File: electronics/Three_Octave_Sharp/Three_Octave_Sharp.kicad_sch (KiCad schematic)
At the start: 156 parts, among them J1 FFC Connector, J1 HRO_TYPE-C-31-M-12, SW1 Key Esc, SW10 Key 9, SW11 Key 0, SW12 Key -, SW13 Key =, SW14 Key \, SW15 Key `, SW16 Key Tab, SW17 Key Q, SW18 Key W, SW19 Key E, SW2 Key 1, SW20 Key R, SW21 Alps_Alpine_SKRP, SW21 Key T, SW22 Alps_Alpine_SKRP, SW22 Key Y, SW23 Key U, SW24 Key I, SW25 Key O, SW26 Key P, SW27 Key [, SW28 Key ], SW29 Key BS, SW3 Key 2, SW30 Key Caps, SW31 Key A, SW32 Key S, SW33 Key D, SW34 Key F, SW35 Key G, SW36 Key H, SW37 Key J, SW38 Key K, SW39 Key L, SW4 Key 3, SW40 Key ;, SW41 Key ', SW42 Key Return, SW43 Key Shift, SW44 Key Z, SW45 Key X, SW46 Key C, SW47 Key V, SW48 Key B, SW49 Key N, SW5 Key 4, SW50 Key M, SW51 Key ,, SW52 Key ., SW53 Key /, SW54 Key Shift, SW55 Key Fn, SW56 Key Ctrl, SW57 Key Opt, SW58 Key Cmd, SW59 Key Space, SW6 Key 5, SW60 Key Cmd, SW61 Key MO(1), SW7 Key 6, SW8 Key 7, SW9 Key 8, U1 AP2112K-3.3, U2 Raspberry_Pi_RP2040, U2 W25Q64JVXGIQ, Y1 12MHz

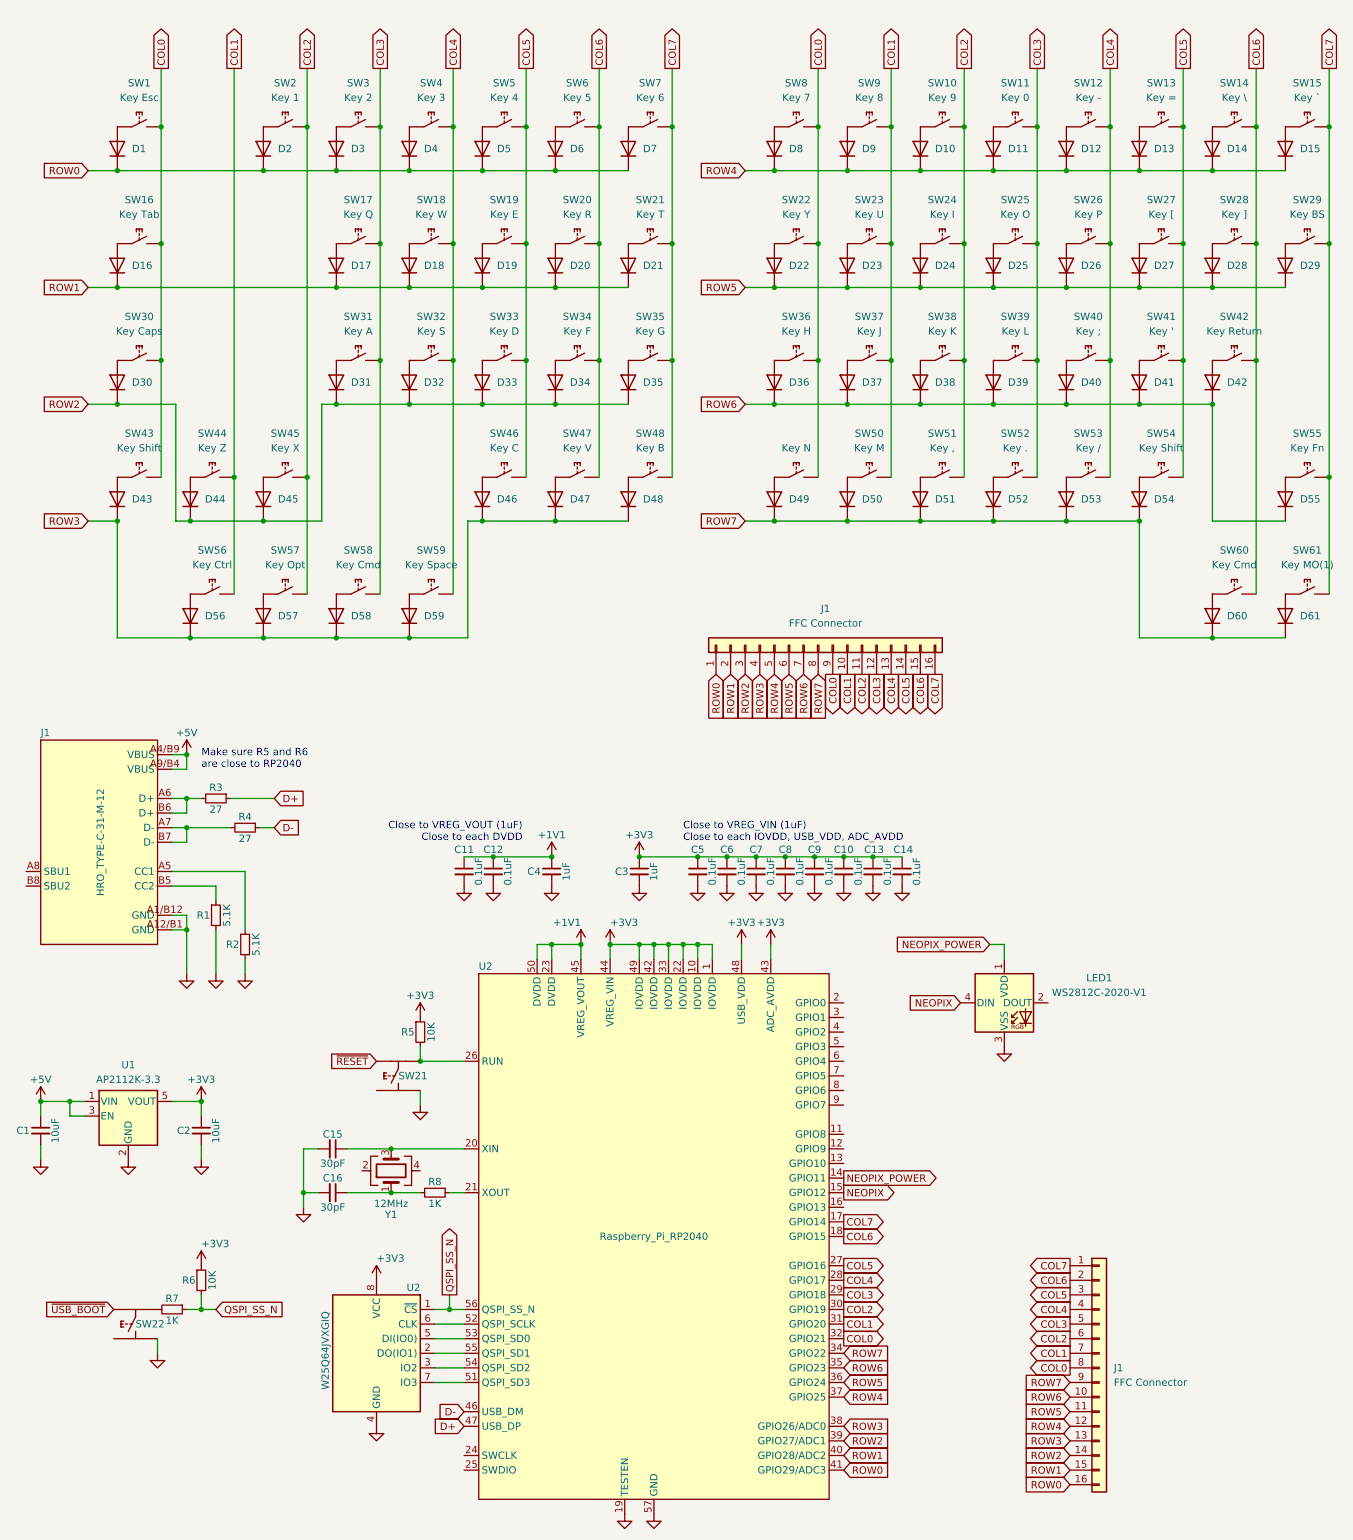
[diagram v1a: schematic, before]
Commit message: Layout keys on PCB
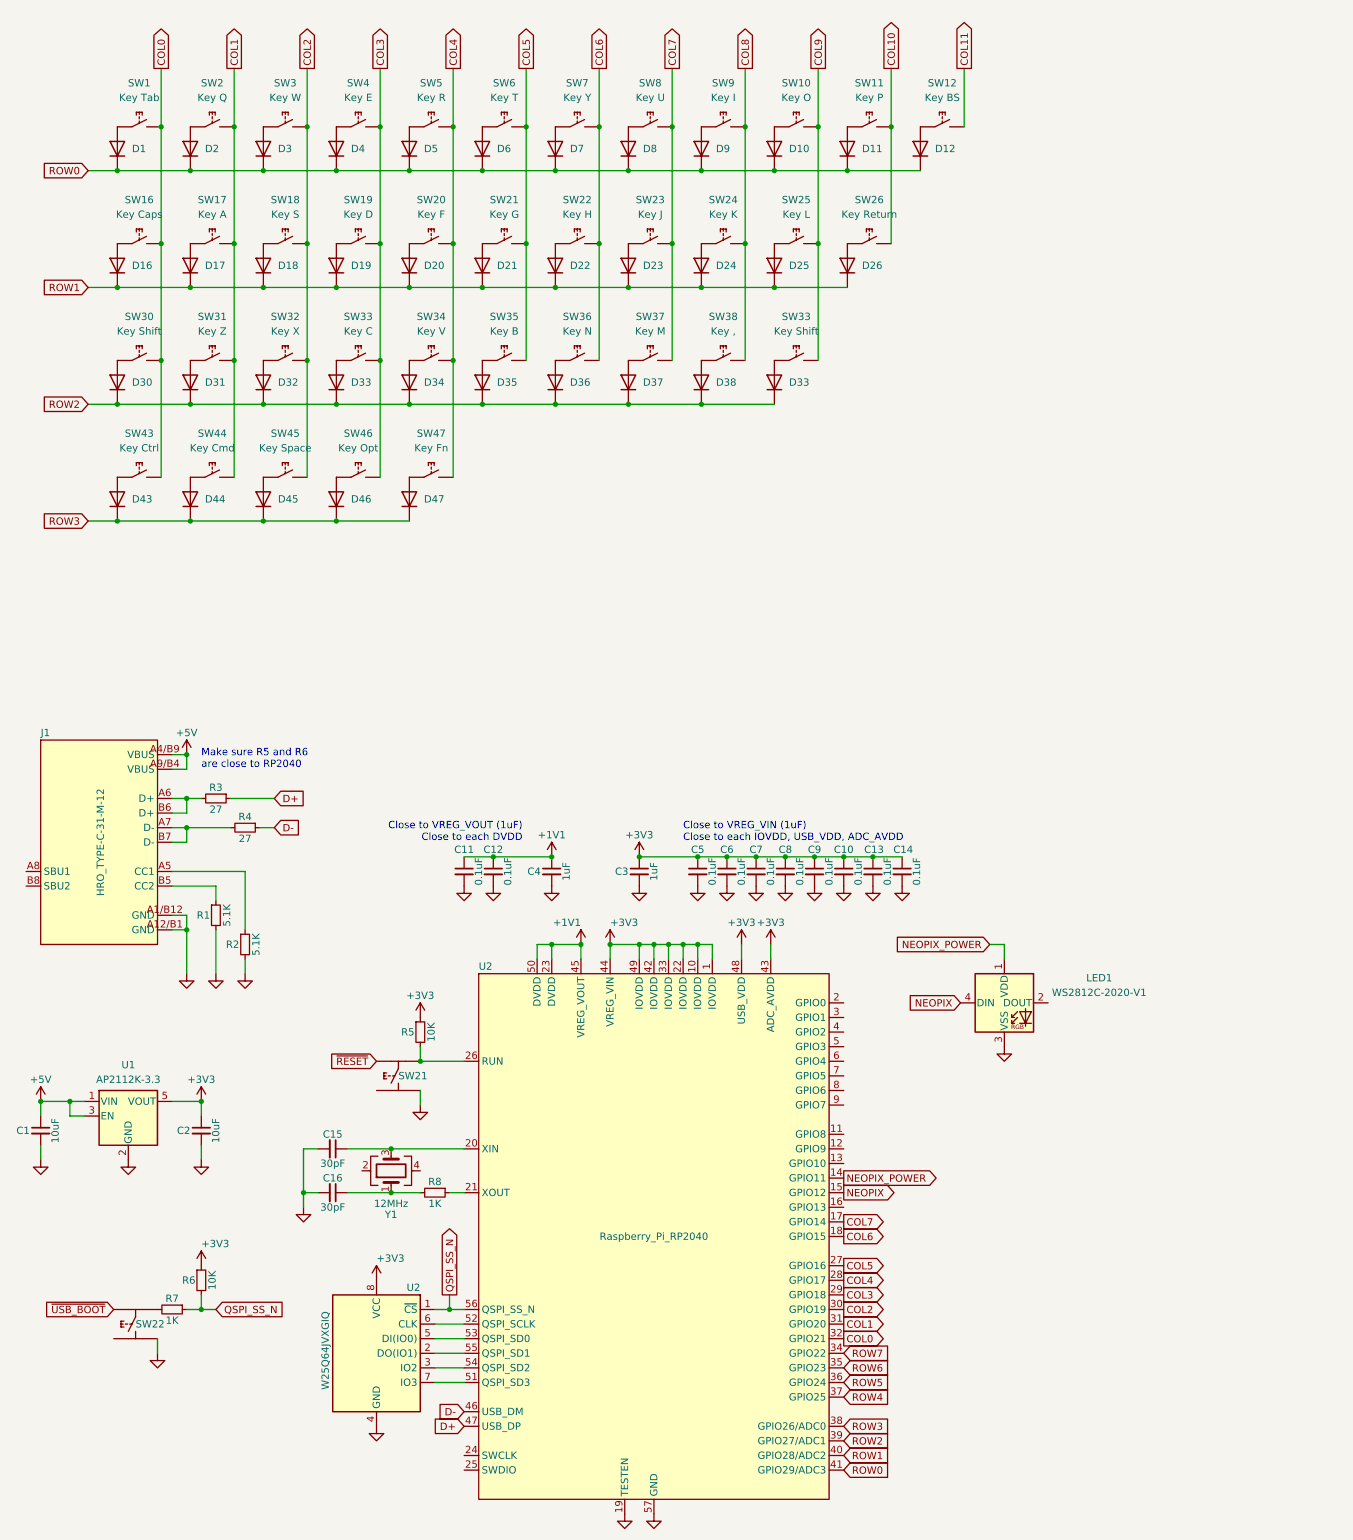
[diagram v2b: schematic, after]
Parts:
- removed D13, D14, D15, D27, D28, D29, D39, D40, D41, D42, D48, D49, D50, D51, D52, D53, D54, D55, D56, D57, D58, D59, D60, D61: 1N4148WS, Project_Library:D_SOD-323F, symbol Diode:1N4148WS
- removed J1 (x2): FFC Connector, Project_Library:JUSHUO_AFC01-S16FCC-00, symbol Connector_Generic:Conn_01x16
- removed SW13: Key =, Project_Library:Hot_Swap_Socket_CPG151101S11, symbol Project_Library:SW_Hot_Swap_Socket
- removed SW14: Key \, Project_Library:Hot_Swap_Socket_CPG151101S11, symbol Project_Library:SW_Hot_Swap_Socket
- removed SW15: Key `, Project_Library:Hot_Swap_Socket_CPG151101S11, symbol Project_Library:SW_Hot_Swap_Socket
- removed SW27: Key [, Project_Library:Hot_Swap_Socket_CPG151101S11, symbol Project_Library:SW_Hot_Swap_Socket
- removed SW28: Key ], Project_Library:Hot_Swap_Socket_CPG151101S11, symbol Project_Library:SW_Hot_Swap_Socket
- removed SW29: Key BS, Project_Library:Hot_Swap_Socket_CPG151101S11, symbol Project_Library:SW_Hot_Swap_Socket
- removed SW39: Key L, Project_Library:Hot_Swap_Socket_CPG151101S11, symbol Project_Library:SW_Hot_Swap_Socket
- removed SW40: Key ;, Project_Library:Hot_Swap_Socket_CPG151101S11, symbol Project_Library:SW_Hot_Swap_Socket
- removed SW41: Key ', Project_Library:Hot_Swap_Socket_CPG151101S11, symbol Project_Library:SW_Hot_Swap_Socket
- removed SW42: Key Return, Project_Library:Hot_Swap_Socket_CPG151101S11, symbol Project_Library:SW_Hot_Swap_Socket
- removed SW48: Key B, Project_Library:Hot_Swap_Socket_CPG151101S11, symbol Project_Library:SW_Hot_Swap_Socket
- removed SW49: Key N, Project_Library:Hot_Swap_Socket_CPG151101S11, symbol Project_Library:SW_Hot_Swap_Socket
- removed SW50: Key M, Project_Library:Hot_Swap_Socket_CPG151101S11, symbol Project_Library:SW_Hot_Swap_Socket
- removed SW51: Key ,, Project_Library:Hot_Swap_Socket_CPG151101S11, symbol Project_Library:SW_Hot_Swap_Socket
- removed SW52: Key ., Project_Library:Hot_Swap_Socket_CPG151101S11, symbol Project_Library:SW_Hot_Swap_Socket
- removed SW53: Key /, Project_Library:Hot_Swap_Socket_CPG151101S11, symbol Project_Library:SW_Hot_Swap_Socket
- removed SW54: Key Shift, Project_Library:Hot_Swap_Socket_CPG151101S11, symbol Project_Library:SW_Hot_Swap_Socket
- removed SW55: Key Fn, Project_Library:Hot_Swap_Socket_CPG151101S11, symbol Project_Library:SW_Hot_Swap_Socket
- removed SW56: Key Ctrl, Project_Library:Hot_Swap_Socket_CPG151101S11, symbol Project_Library:SW_Hot_Swap_Socket
- removed SW57: Key Opt, Project_Library:Hot_Swap_Socket_CPG151101S11, symbol Project_Library:SW_Hot_Swap_Socket
- removed SW58, SW60: Key Cmd, Project_Library:Hot_Swap_Socket_CPG151101S11, symbol Project_Library:SW_Hot_Swap_Socket
- removed SW59: Key Space, Project_Library:Hot_Swap_Socket_CPG151101S11, symbol Project_Library:SW_Hot_Swap_Socket
- removed SW61: Key MO(1), Project_Library:Hot_Swap_Socket_CPG151101S11, symbol Project_Library:SW_Hot_Swap_Socket
- added D33: 1N4148WS, Project_Library:D_SOD-323F, symbol Diode:1N4148WS
- added SW33: Key Shift, Project_Library:Hot_Swap_Socket_CPG151101S11, symbol Project_Library:SW_Hot_Swap_Socket
- SW1: value Key Esc -> Key Tab
- SW10: value Key 9 -> Key O
- SW11: value Key 0 -> Key P
- SW12: value Key - -> Key BS
- SW16: value Key Tab -> Key Caps
- SW17: value Key Q -> Key A
- SW18: value Key W -> Key S
- SW19: value Key E -> Key D
- SW2: value Key 1 -> Key Q
- SW20: value Key R -> Key F
- SW21: value Key T -> Key G
- SW22: value Key Y -> Key H
- SW23: value Key U -> Key J
- SW24: value Key I -> Key K
- SW25: value Key O -> Key L
- SW26: value Key P -> Key Return
- SW3: value Key 2 -> Key W
- SW30: value Key Caps -> Key Shift
- SW31: value Key A -> Key Z
- SW32: value Key S -> Key X
- SW33: value Key D -> Key C
- SW34: value Key F -> Key V
- SW35: value Key G -> Key B
- SW36: value Key H -> Key N
- SW37: value Key J -> Key M
- SW38: value Key K -> Key ,
- SW4: value Key 3 -> Key E
- SW43: value Key Shift -> Key Ctrl
- SW44: value Key Z -> Key Cmd
- SW45: value Key X -> Key Space
- SW46: value Key C -> Key Opt
- SW47: value Key V -> Key Fn
- SW5: value Key 4 -> Key R
- SW6: value Key 5 -> Key T
- SW7: value Key 6 -> Key Y
- SW8: value Key 7 -> Key U
- SW9: value Key 8 -> Key I
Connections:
- net COL0: no longer SW22.2, SW36.2, SW8.2
- net COL1: now also SW17.2, SW2.2, SW31.2; no longer SW23.2, SW37.2, SW9.2
- net COL2: now also SW18.2, SW3.2, SW32.2; no longer SW10.2, SW2.2, SW24.2, SW38.2
- net COL3: now also SW19.2, SW33.2, SW4.2, SW46.2; no longer SW11.2, SW17.2, SW25.2, SW3.2, SW31.2
- net COL4: now also SW20.2, SW34.2, SW47.2, SW5.2; no longer SW12.2, SW18.2, SW26.2, SW32.2, SW4.2
- net COL5: now also SW21.2, SW35.2, SW6.2; no longer SW19.2, SW33.2, SW46.2, SW5.2
- net COL6: now also SW22.2, SW36.2, SW7.2; no longer SW20.2, SW34.2, SW47.2, SW6.2
- net COL7: now also SW23.2, SW37.2, SW8.2; no longer SW21.2, SW35.2, SW7.2
- net ROW0: now also D10.1 (K), D11.1 (K), D12.1 (K), D8.1 (K), D9.1 (K)
- net ROW1: now also D22.1 (K), D23.1 (K), D24.1 (K), D25.1 (K), D26.1 (K)
- net ROW2: now also D36.1 (K), D37.1 (K), D38.1 (K), D33.1 (K); no longer D44.1 (K), D45.1 (K)
- net ROW3: now also D44.1 (K), D45.1 (K)
- net ROW4: no longer D10.1 (K), D11.1 (K), D12.1 (K), D8.1 (K), D9.1 (K)
- net ROW5: no longer D22.1 (K), D23.1 (K), D24.1 (K), D25.1 (K), D26.1 (K)
- net ROW6: no longer D36.1 (K), D37.1 (K), D38.1 (K)
- new net: D33.2 (A), SW33.1
- new net COL10: SW11.2, SW26.2
- new net COL11: SW12.2
- new net COL8: SW24.2, SW38.2, SW9.2
- new net COL9: SW10.2, SW25.2, SW33.2
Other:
- moved on the sheet: D10, D11, D12, D17, D18, D19, D2, D20, D21, D22, D23, D24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

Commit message: WIP: Update schematic and PCB design
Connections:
- net ROW4 is gone; now on net COL0: U2.37 (GPIO25)
- net ROW5 is gone; now on net COL1: U2.36 (GPIO24)
- net ROW6 is gone; now on net COL2: U2.35 (GPIO23)
- net ROW7 is gone; now on net COL3: U2.34 (GPIO22)
- net COL0: no longer U2.32 (GPIO21)
- net COL1: no longer U2.31 (GPIO20)
- net COL10: now also U2.3 (GPIO1)
- net COL11: now also U2.2 (GPIO0)
- net COL2: no longer U2.30 (GPIO19)
- net COL3: no longer SW46.2, U2.29 (GPIO18)
- net COL4: now also U2.32 (GPIO21); no longer SW47.2, U2.28 (GPIO17)
- net COL5: now also U2.31 (GPIO20); no longer U2.27 (GPIO16)
- net COL6: now also U2.7 (GPIO5); no longer U2.18 (GPIO15)
- net COL7: now also U2.6 (GPIO4); no longer U2.17 (GPIO14)
- net COL8: now also SW46.2, U2.5 (GPIO3)
- net COL9: now also SW47.2, U2.4 (GPIO2)
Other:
- moved on the sheet: D46, D47, SW46, SW47
